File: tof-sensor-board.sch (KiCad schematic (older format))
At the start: 38 parts, among them IC1 TLV710, U1 STM32F042C6T6, U2 LTC2875, U3 VL6180X, X1 16MHz

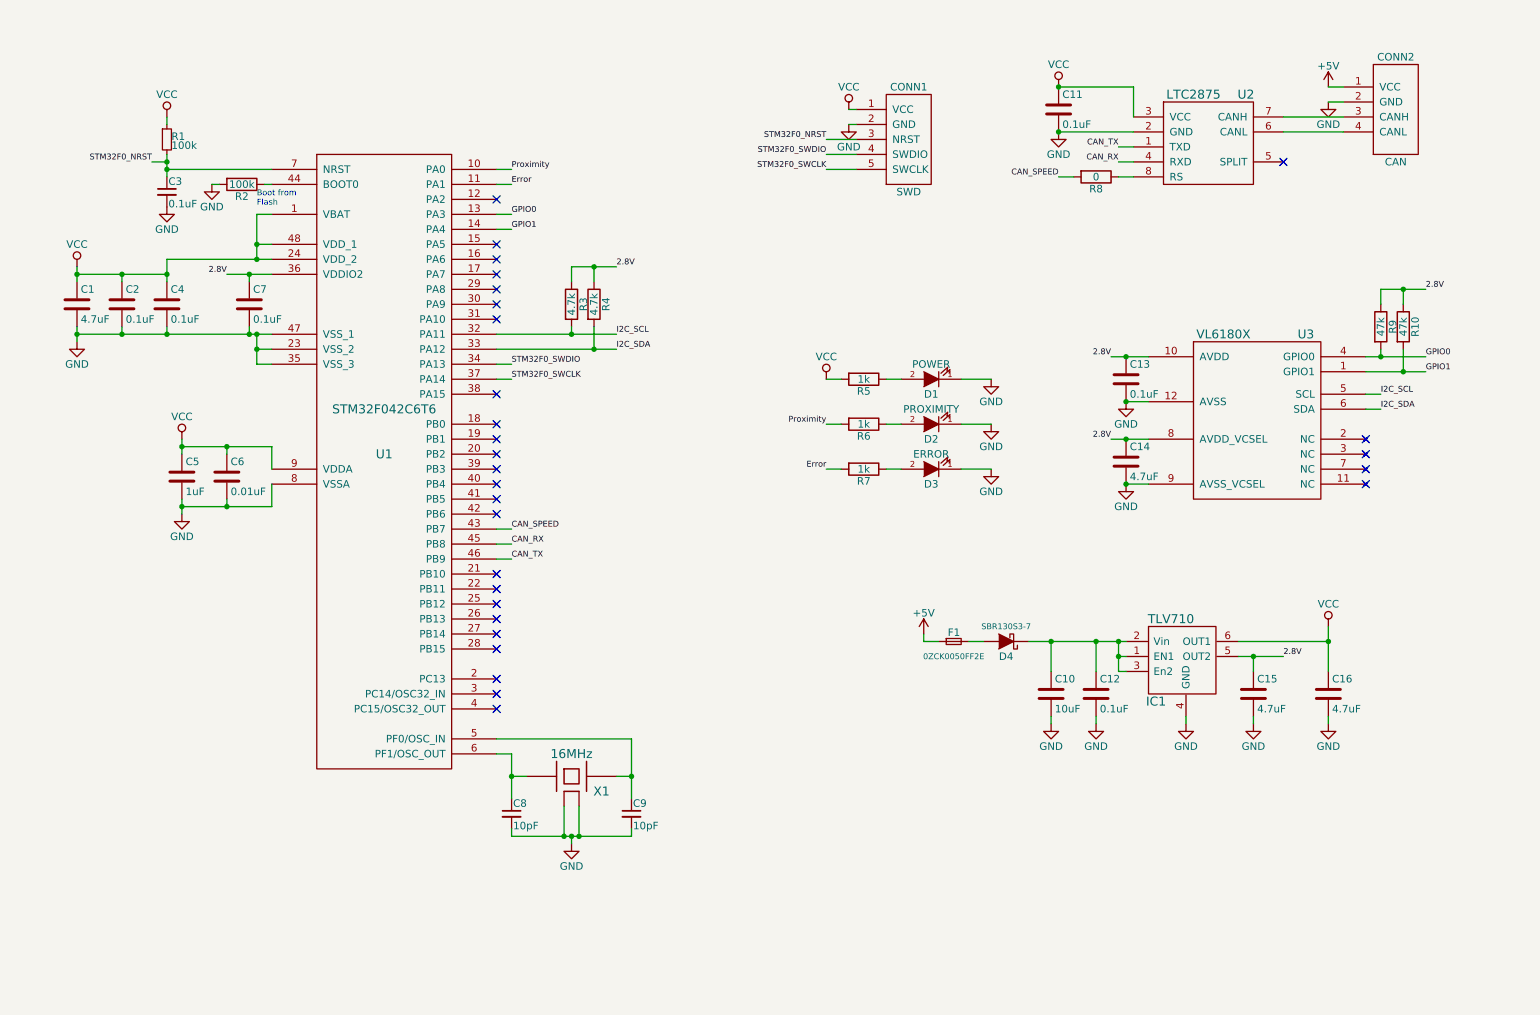
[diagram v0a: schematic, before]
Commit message: Duplicate CAN connector to allow daisy chain wiring
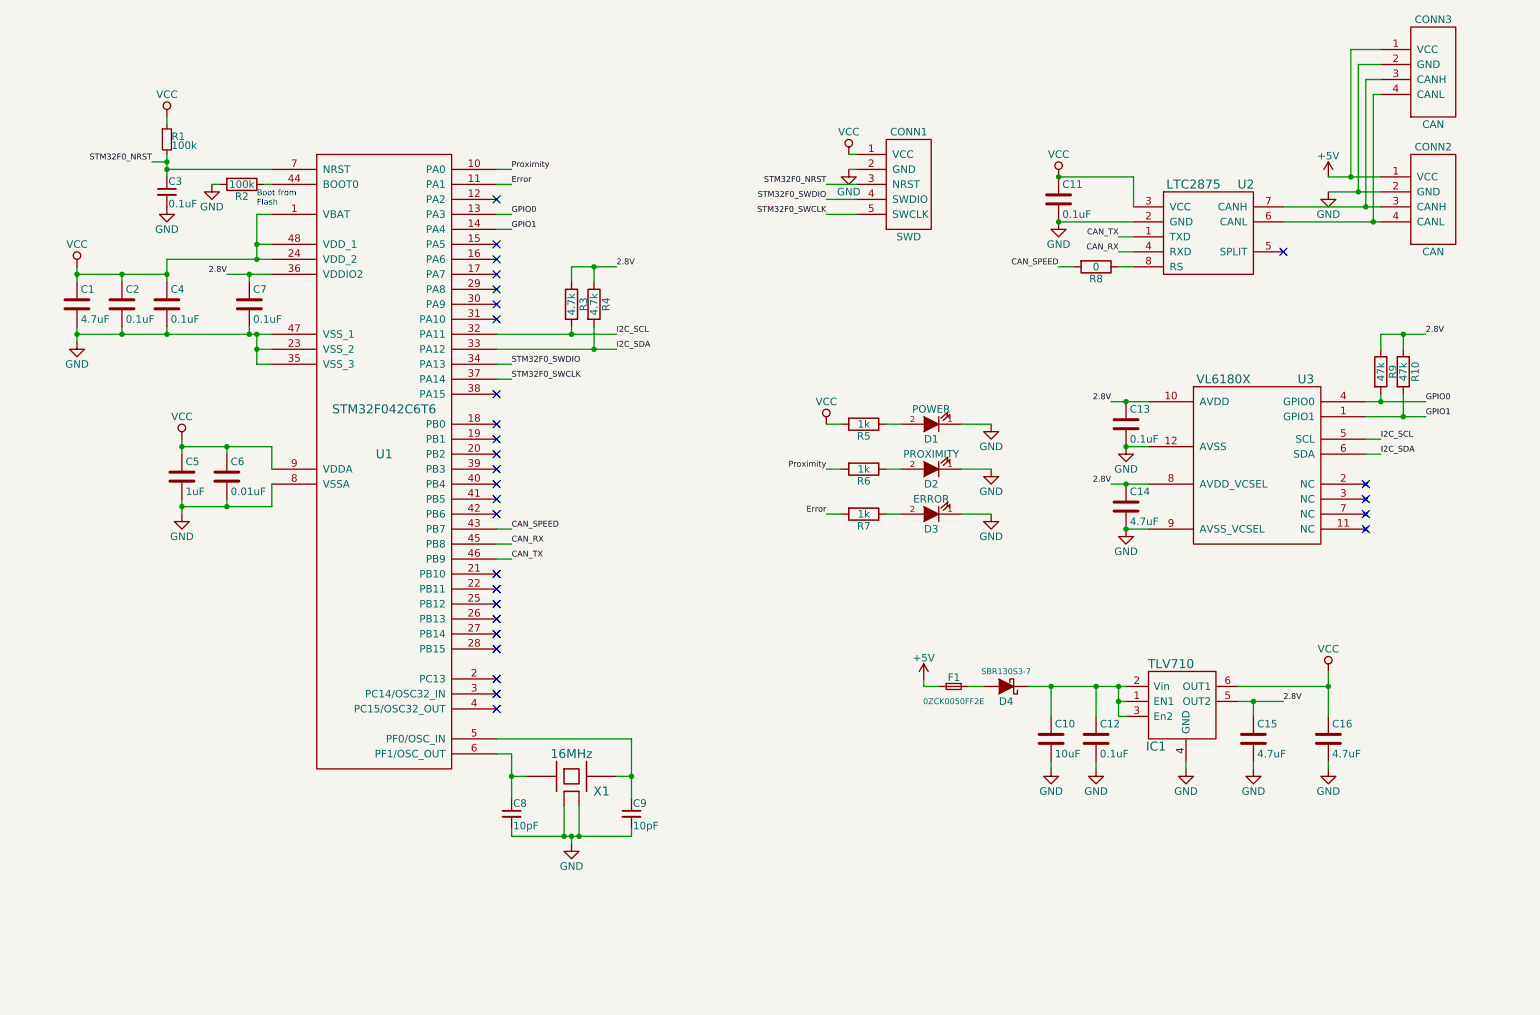
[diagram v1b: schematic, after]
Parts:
- added CONN3: CAN, MODULE, symbol CAN
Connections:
- net +5V: now also CONN3.1 (VCC)
- net GND: now also CONN3.2 (GND), CONN3.MECH (GND)
- net at CONN2.4 (CANL), U2.6 (CANL): now also CONN3.4 (CANL)
- net at CONN2.3 (CANH), U2.7 (CANH): now also CONN3.3 (CANH)
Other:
- moved on the sheet: C10, C11, C12, C13, C14, C15, C16, CONN1, CONN2, D1, D2, D3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

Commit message: Netlist
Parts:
- C1, C10, C11, C12, C13, C14, C15, C16, C2, C3, C4, C5, C6, C7, C8, C9: footprint (none) -> Capacitors_SMD:C_0402
- CONN1: footprint MODULE -> _connectors:_Pin2mm_5z
- CONN2, CONN3: footprint MODULE -> _connectors:_Molex-PicoBlade-SMD-4
- D1, D2, D3: footprint (none) -> _std:_0603
- D4: footprint (none) -> _std:_SOD-323
- F1: footprint (none) -> Capacitors_SMD:C_0805
- IC1: footprint (none) -> cvra:CVRA-PWSON-N6
- R1, R10, R2, R3, R4, R5, R6, R7, R8, R9: footprint (none) -> Resistors_SMD:R_0402
- U1: footprint MODULE -> _lqfp:_LQFP48
- U2: footprint (none) -> Housings_DFN_QFN:DFN-8-1EP_3x3mm_Pitch0.5mm
- U3: footprint (none) -> _sensors:VL6180X
- X1: footprint (none) -> _div:_TSX-3225-SMD-XTAL

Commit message: PCB
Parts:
- CONN1: footprint _connectors:_Pin2mm_5z -> _connectors:_SoldarPad2mm_5
- U3: footprint _sensors:VL6180X -> _sensors:VL6180X_EdgeMount
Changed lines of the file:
@@
 F 0 "U3" H 9600 4100 59  0000 C CNN
 F 1 "VL6180X" H 9050 4100 59  0000 C CNN
-F 2 "_sensors:VL6180X" H 9150 4300 39  0001 C CNN
+F 2 "_sensors:VL6180X_EdgeMount" H 9150 4300 39  0001 C CNN
 F 3 "" H 9150 4300 39  0000 C CNN
 	1    8950 3700
@@
 F 0 "CONN1" H 6950 2350 50  0000 C CNN
 F 1 "SWD" H 6950 1650 50  0000 C CNN
-F 2 "_connectors:_Pin2mm_5z" H 6950 1850 50  0001 C CNN
+F 2 "_connectors:_SoldarPad2mm_5" H 6950 1850 50  0001 C CNN
 F 3 "DOCUMENTATION" H 6950 1850 50  0001 C CNN
 	1    6950 2000

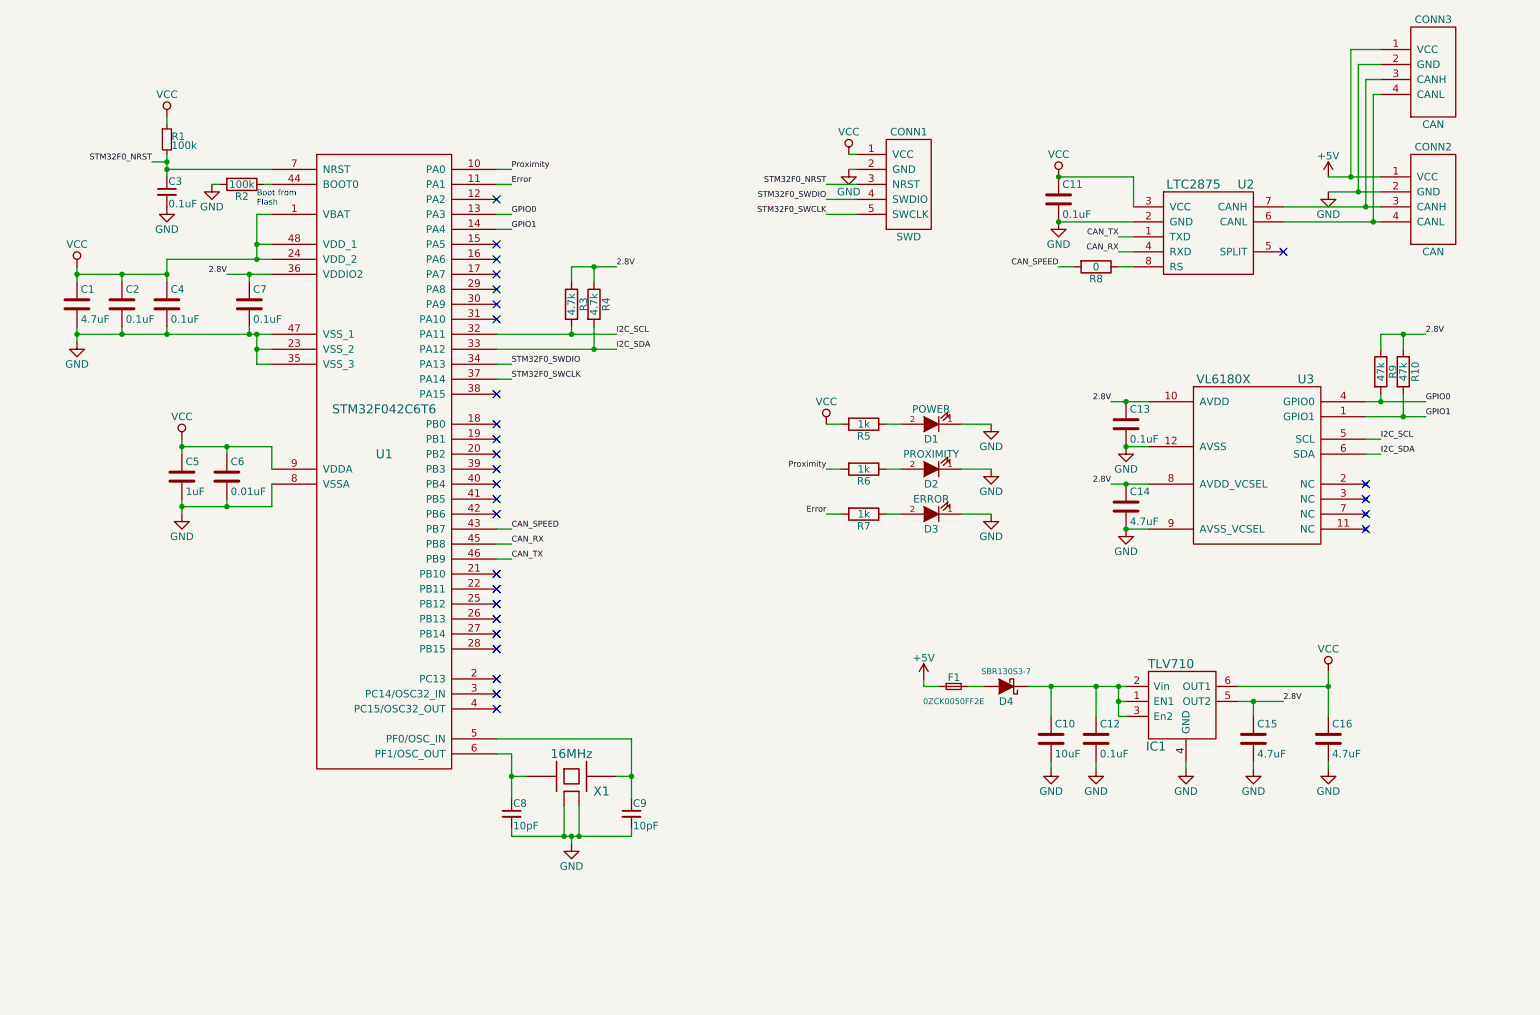
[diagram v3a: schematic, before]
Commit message: Switch to VL53L0X and QFN32 STM32f302
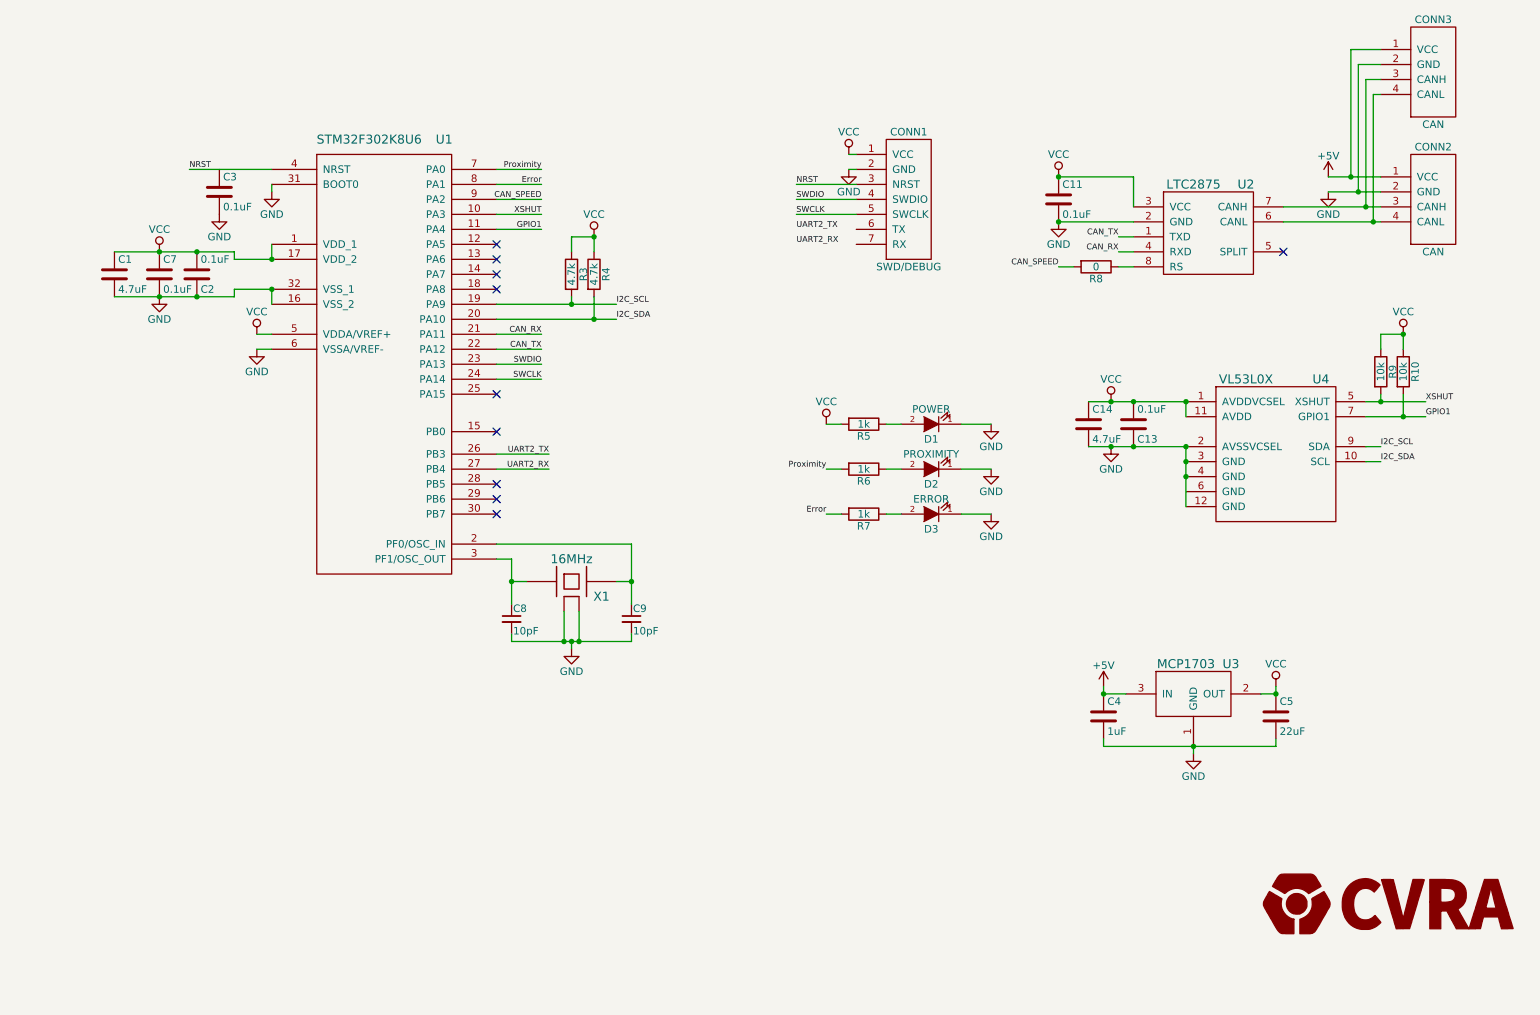
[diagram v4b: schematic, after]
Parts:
- removed C10: 10uF, Capacitors_SMD:C_0402, symbol C
- removed C12: 0.1uF, Capacitors_SMD:C_0402, symbol C
- removed C15, C16: 4.7uF, Capacitors_SMD:C_0402, symbol C
- removed C3: 0.1uF, Capacitors_SMD:C_0402, symbol C_Small
- removed C6: 0.01uF, Capacitors_SMD:C_0402, symbol C
- removed CONN1: SWD, _connectors:_SoldarPad2mm_5, symbol SWD
- removed D4: SBR130S3-7, _std:_SOD-323, symbol D_Schottky
- removed F1: 0ZCK0050FF2E, Capacitors_SMD:C_0805, symbol F_Small
- removed IC1: TLV710, cvra:CVRA-PWSON-N6, symbol TLV710
- removed R1: 100k, Resistors_SMD:R_0402, symbol R_Small
- removed R2: 100k, Resistors_SMD:R_0402, symbol R
- removed U1: STM32F042C6T6, _lqfp:_LQFP48, symbol STM32F042C6T6
- removed U3: VL6180X, _sensors:VL6180X_EdgeMount, symbol VL6180X
- added C3: 0.1uF, Capacitors_SMD:C_0402, symbol C
- added CONN1: SWD/DEBUG, Connectors_Molex:Connector_Molex_PicoBlade_53048-0710, symbol SWD/DEBUG
- added U1: STM32F302K8U6, Housings_DFN_QFN:QFN-32-1EP_5x5mm_Pitch0.5mm, symbol STM32F302K8U6
- added U3: MCP1703, symbol MCP1703
- added U4: VL53L0X, symbol VL53L0X
- C1: footprint Capacitors_SMD:C_0402 -> Capacitors_SMD:C_0603
- C4: value 0.1uF -> 1uF; footprint Capacitors_SMD:C_0402 -> (none)
- C5: value 1uF -> 22uF; footprint Capacitors_SMD:C_0402 -> (none)
- R10, R9: value 47k -> 10k
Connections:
- net +5V: now also C4.1, U3.3 (IN)
- net CAN_RX: now also U1.21 (PA11)
- net CAN_SPEED: now also U1.9 (PA2)
- net CAN_TX: now also U1.22 (PA12)
- net Error: now also U1.8 (PA1)
- net GND: now also C13.1, C2.1, C3.2, CONN1.2 (GND), CONN1.MECH (GND), U1.16 (VSS_2), U1.31 (BOOT0), U1.32 (VSS_1), U1.6 (VSSA/VREF-), U3.1 (GND), U4.12 (GND), U4.2 (AVSSVCSEL), U4.3 (GND), U4.4 (GND); no longer C13.2, C2.2
- net GPIO1: now also U1.11 (PA4), U4.7 (GPIO1)
- net I2C_SCL: now also U1.19 (PA9), U4.9 (SDA)
- net I2C_SDA: now also U1.20 (PA10), U4.10 (SCL)
- net Proximity: now also U1.7 (PA0)
- net VCC: now also C13.2, C14.1, C2.2, C7.1, R10.1, R3.1, R4.1, R9.1, CONN1.1 (VCC), U1.1 (VDD_1), U1.17 (VDD_2), U1.5 (VDDA/VREF+), U3.2 (OUT), U4.1 (AVDDVCSEL), U4.11 (AVDD); no longer C2.1, C4.1
- net at C8.1, X1.1: now also U1.3 (PF1/OSC_OUT)
- net at C9.1, X1.3: now also U1.2 (PF0/OSC_IN)
- removed net 2.8V: C13.1, C14.1, C7.1, R10.1, R3.1, R4.1, R9.1
- net GPIO0 renamed XSHUT
- net XSHUT: now also U1.10 (PA3), U4.5 (XSHUT)
- new net NRST: CONN1.3 (NRST), U1.4 (NRST)
- new net SWCLK: CONN1.5 (SWCLK), U1.24 (PA14)
- new net SWDIO: CONN1.4 (SWDIO), U1.23 (PA13)
- new net UART2_RX: U1.27 (PB4)
- new net UART2_TX: U1.26 (PB3)
- no-connect marks 29 -> 10
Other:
- note removed: "Boot from \nFlash"
- moved on the sheet: C13, C14, C2, C7, C8, C9, R3, R4, X1

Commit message: Fix I2C connection, remove power LED
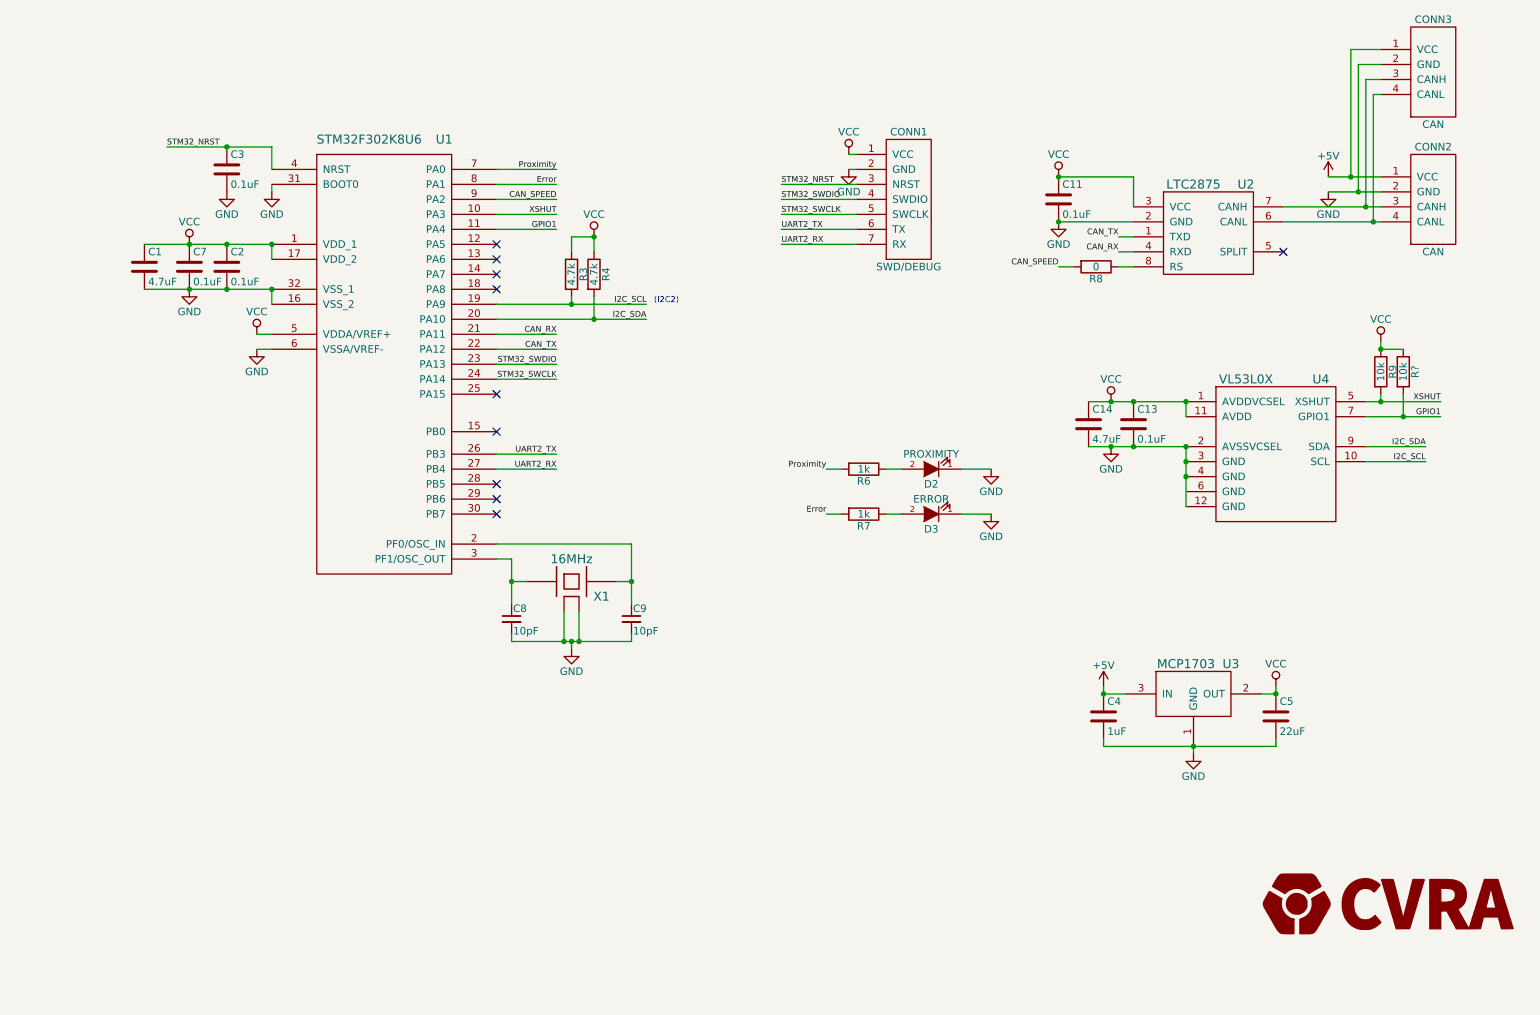
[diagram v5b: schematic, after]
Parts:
- removed D1: POWER, _std:_0603, symbol LED
- removed R10: 10k, Resistors_SMD:R_0402, symbol R
- removed R5: 1k, Resistors_SMD:R_0402, symbol R
- added R?: 10k, Resistors_SMD:R_0402, symbol R
- C13: footprint Capacitors_SMD:C_0402 -> (none)
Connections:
- net NRST is gone; now on net STM32_NRST: CONN1.3 (NRST), U1.4 (NRST)
- net GND: now also C13.2, C2.2; no longer C13.1, C2.1
- net GPIO1: now also R?.2
- net I2C_SCL: now also U4.10 (SCL); no longer U4.9 (SDA)
- net I2C_SDA: now also U4.9 (SDA); no longer U4.10 (SCL)
- net UART2_RX: now also CONN1.7 (RX)
- net UART2_TX: now also CONN1.6 (TX)
- net VCC: now also C13.1, C2.1, R?.1; no longer C13.2, C2.2
- net STM32_NRST: now reaches C3.1
- net SWCLK renamed STM32_SWCLK
- net SWDIO renamed STM32_SWDIO
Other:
- note added: "(I2C2)"
- moved on the sheet: C1, C2, C3, C7
